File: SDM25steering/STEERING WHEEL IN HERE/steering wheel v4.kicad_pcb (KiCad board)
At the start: 4 copper layers, 162.2 x 126.4 mm, 125 parts, among them J1 JST_EH_S2B-EH_1x02_P2.50mm_Ho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, J2 JST_EH_S2B-EH_1x02_P2.50mm_Ho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, J3 Conn_01x04_Socket, J4 Conn_ARM_SWD_TagConnect_TC2030, J5 USB_B_Micro, U1 STM32F405RGT6, U2 MIC37100-3.3WS, U3 SN65HVD230, U4 TLC59108F, U5 ADR425BRZ, U6 24LC01BT-E/LT, U6 TPS2116, U7 ADC128S102, U8 USBLC6-2SC6, Y1 12MHz

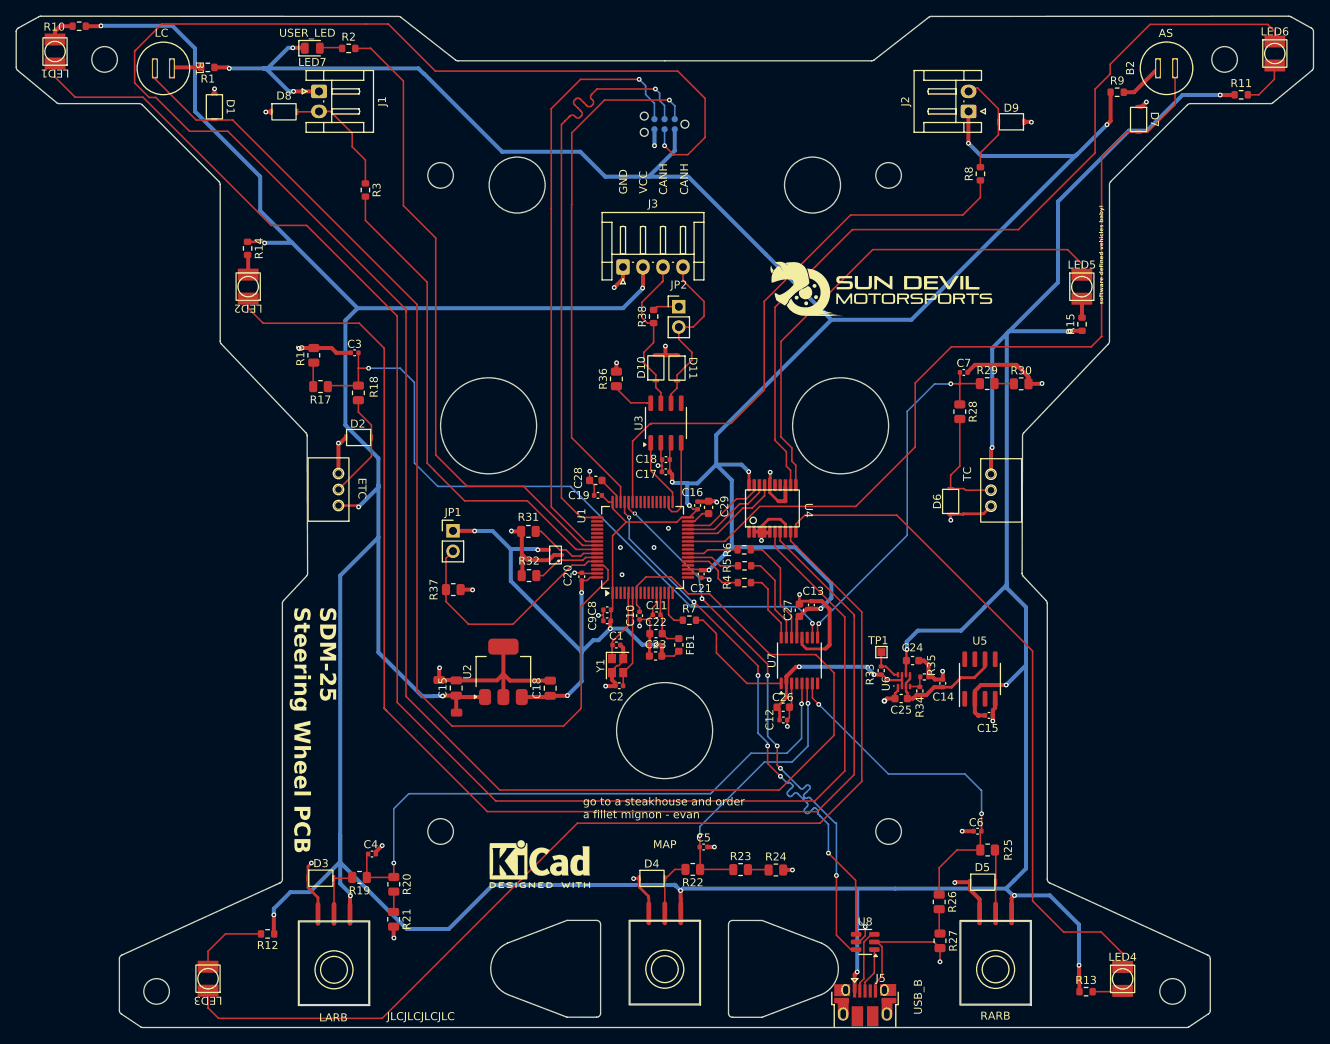
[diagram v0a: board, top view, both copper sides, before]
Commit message: SDM-24 Logger TVS diodes
TVS protection added on all analog inputs. Also built out for manufacture files.
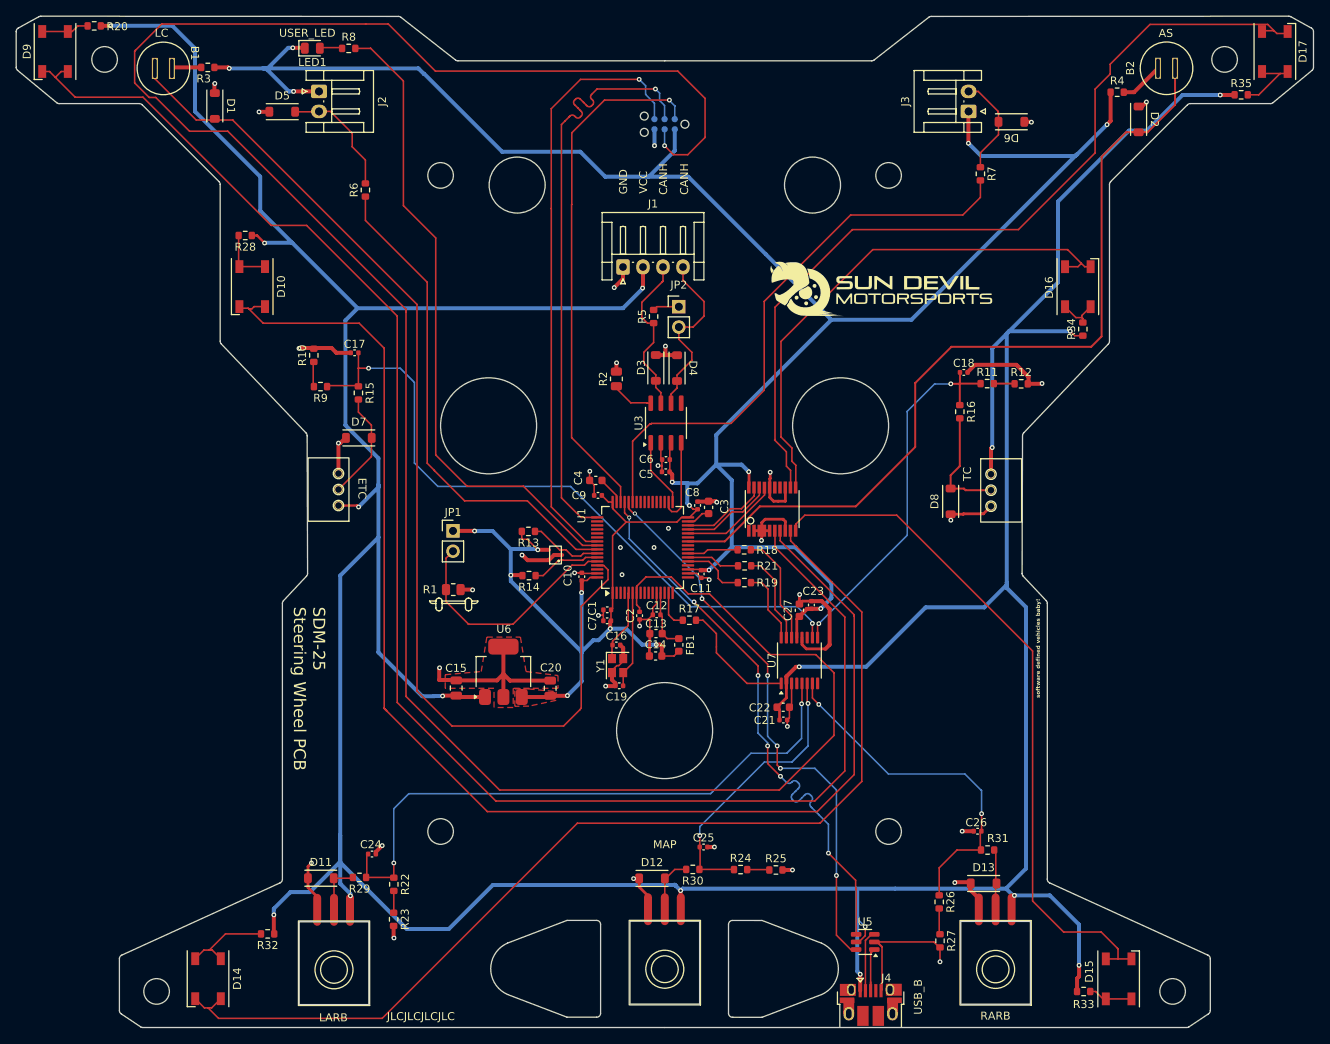
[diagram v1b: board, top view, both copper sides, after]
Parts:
- removed ? (x2): , 
- removed the C14 at (186.7, 109.0)
- removed the C15 at (192.5, 113.0)
- removed the C24 at (182.9, 106.1)
- removed the C25 at (181.5, 110.9)
- removed the R33 at (179.0, 107.4)
- removed the R34 at (183.8, 109.9)
- removed the R35 at (184.4, 108.2)
- removed REF**: KiCad-Logo2_5mm_SilkScreen, Symbol:KiCad-Logo2_5mm_SilkScreen
- removed TP1: ST_5VA, TestPoint:TestPoint_Pad_1.0x1.0mm
- removed the U4 at (165.4, 87.1)
- removed the U5 at (191.3, 108.4)
- removed the U6 at (180.4, 108.7)
- added TLC59108F1: U4, Library:TLC59108F, F.Cu at (165.4, 87.2)
- C17: renamed from C3; value 100nF -> 100n
- C18: renamed from C7; value 100nF -> 100n
- C24: renamed from C4; value 100nF -> 100n
- C25: renamed from C5; value 100nF -> 100n
- C26: renamed from C6; value 100nF -> 100n
- D1: footprint TVS Diode:SOD-123FL -> Library:SOD-123FL
- D10: renamed from LED2; value green -> LTST-C235KGKRKT; footprint LED:LR T66F-AABB-1-1 -> LED_SMD:LED_Cree-PLCC4_5x5mm_CW
- D11: renamed from D3; footprint TVS Diode:SOD-123FL -> Library:SOD-123FL
- D12: renamed from D4; footprint TVS Diode:SOD-123FL -> Library:SOD-123FL
- D13: renamed from D5; footprint TVS Diode:SOD-123FL -> Library:SOD-123FL
- D14: renamed from LED3; value green -> LTST-C235KGKRKT; footprint LED:LR T66F-AABB-1-1 -> LED_SMD:LED_Cree-PLCC4_5x5mm_CW
- D15: renamed from LED4; value green -> LTST-C235KGKRKT; footprint LED:LR T66F-AABB-1-1 -> LED_SMD:LED_Cree-PLCC4_5x5mm_CW
- D16: renamed from LED5; value green -> LTST-C235KGKRKT; footprint LED:LR T66F-AABB-1-1 -> LED_SMD:LED_Cree-PLCC4_5x5mm_CW
- D17: renamed from LED6; value blue -> LTST-C235KGKRKT; footprint LED:LR T66F-AABB-1-1 -> LED_SMD:LED_Cree-PLCC4_5x5mm_CW
- D2: renamed from D7; footprint TVS Diode:SOD-123FL -> Library:SOD-123FL
- D3: renamed from D10; footprint TVS Diode:SOD-123FL -> Library:SOD-123FL
- D4: renamed from D11; footprint TVS Diode:SOD-123FL -> Library:SOD-123FL
- D5: renamed from D8; footprint TVS Diode:SOD-123FL -> Library:SOD-123FL
- D6: renamed from D9; footprint TVS Diode:SOD-123FL -> Library:SOD-123FL
- D7: renamed from D2; footprint TVS Diode:SOD-123FL -> Library:SOD-123FL
- D8: renamed from D6; footprint TVS Diode:SOD-123FL -> Library:SOD-123FL
- D9: renamed from LED1; value red -> LTST-C235KGKRKT; footprint LED:LR T66F-AABB-1-1 -> LED_SMD:LED_Cree-PLCC4_5x5mm_CW
- J2: renamed from J1; value JST_EH_S2B-EH_1x02_P2.50mm_Horizontal -> Conn_01x02
- J3: renamed from J2; value JST_EH_S2B-EH_1x02_P2.50mm_Horizontal -> Conn_01x02
- POT4, POT5: footprint Dial Potentiometer:P081N-271F2CBR10K -> Library:P081N-271F2CBR10K
- R10: renamed from R16; value 1000 -> 1k; footprint Resistor_SMD:R_0805_2012Metric -> Resistor_SMD:R_0603_1608Metric
- R11: renamed from R29; value 1000 -> 1k; footprint Resistor_SMD:R_0805_2012Metric -> Resistor_SMD:R_0603_1608Metric
- R12: renamed from R30; value 1000 -> 1k; footprint Resistor_SMD:R_0805_2012Metric -> Resistor_SMD:R_0603_1608Metric
- R13: renamed from R31; footprint Resistor_SMD:R_0805_2012Metric -> Resistor_SMD:R_0603_1608Metric
- R14: renamed from R32; footprint Resistor_SMD:R_0805_2012Metric -> Resistor_SMD:R_0603_1608Metric
- R15: renamed from R18; value 1000 -> 1k; footprint Resistor_SMD:R_0805_2012Metric -> Resistor_SMD:R_0603_1608Metric
- R16: renamed from R28; value 1000 -> 1k; footprint Resistor_SMD:R_0805_2012Metric -> Resistor_SMD:R_0603_1608Metric
- R22: renamed from R20; value 1000 -> 1k; footprint Resistor_SMD:R_0805_2012Metric -> Resistor_SMD:R_0603_1608Metric
- R23: renamed from R21; value 1000 -> 1k; footprint Resistor_SMD:R_0805_2012Metric -> Resistor_SMD:R_0603_1608Metric
- R24: renamed from R23; value 1000 -> 1k; footprint Resistor_SMD:R_0805_2012Metric -> Resistor_SMD:R_0603_1608Metric
- R25: renamed from R24; value 1000 -> 1k; footprint Resistor_SMD:R_0805_2012Metric -> Resistor_SMD:R_0603_1608Metric
- R26, R27: value 1000 -> 1k; footprint Resistor_SMD:R_0805_2012Metric -> Resistor_SMD:R_0603_1608Metric
- R29: renamed from R19; value 1000 -> 1k; footprint Resistor_SMD:R_0805_2012Metric -> Resistor_SMD:R_0603_1608Metric
- R30: renamed from R22; value 1000 -> 1k; footprint Resistor_SMD:R_0805_2012Metric -> Resistor_SMD:R_0603_1608Metric
- R31: renamed from R25; value 1000 -> 1k; footprint Resistor_SMD:R_0805_2012Metric -> Resistor_SMD:R_0603_1608Metric
- R9: renamed from R17; value 1000 -> 1k; footprint Resistor_SMD:R_0805_2012Metric -> Resistor_SMD:R_0603_1608Metric
- moved R20 1.88 mm to (80.6, 26.8)
- moved R28 1.64 mm to (99.5, 53.0), turned to 180 degrees
- moved J4 0.70 mm to (177.7, 149.2)
- moved R34 0.62 mm to (204.2, 64.7)
- moved D10 0.50 mm to (100.4, 59.4), turned to 90 degrees
- moved D15 0.50 mm to (208.7, 145.9), turned to -90 degrees
- moved D16 0.50 mm to (203.6, 59.4), turned to -90 degrees
- moved R33 0.31 mm to (204.3, 147.5)
- moved D17 0.25 mm to (228.2, 30.0), turned to -90 degrees
- moved D5 0.22 mm to (104.1, 37.5)
- moved D13 0.19 mm to (191.8, 134.0)
- moved D1 0.12 mm to (95.7, 36.8)
- moved D7 0.06 mm to (113.7, 78.3)
- turned D14 to 90 degrees
- turned D9 to 90 degrees
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- renumbered C8 to C1, C20 to C10, C21 to C11, C11 to C12, C22 to C13, C23 to C14, C1 to C16, C2 to C19, C10 to C2, C18 to C20, C12 to C21, C26 to C22, C13 to C23, C29 to C3, C28 to C4, C17 to C5, C18 to C6, C9 to C7, C16 to C8, C19 to C9, H5 to H2, H2 to H3, H6 to H4, H3 to H5, H7 to H6, H4 to H7, J3 to J1, J5 to J4, J4 to J5, LED7 to LED1, R37 to R1, R7 to R17, R6 to R18, R4 to R19, R36 to R2, R10 to R20, R5 to R21, R14 to R28, R1 to R3, R12 to R32, R13 to R33, R15 to R34, R11 to R35, R9 to R4, R38 to R5, R3 to R6, R8 to R7, R2 to R8, U6 to U4, U8 to U5, U2 to U6
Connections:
- net I2C1_SCL renamed /I2C1_SCL
- net I2C1_SDA renamed /I2C1_SDA
- net net1 renamed Net-(R22-Pad2)
- net net2 renamed Net-(R24-Pad2)
- net net3 renamed Net-(R26-Pad2)
- net net5 renamed Net-(R11-Pad2)
- net net6 renamed Net-(R10-Pad1)
- C21 pad 1: +5VA -> VCC
- C22 pad 1: +5VA -> VCC
- D10 pad 2: Net-(D12-A) -> Net-(D10-A1)
- D14 pad 2: Net-(D13-A) -> Net-(D14-A1)
- D15 pad 2: Net-(D14-A) -> Net-(D15-A1)
- D16 pad 2: Net-(D16-A) -> Net-(D16-A1)
- D17 pad 2: Net-(D15-A) -> Net-(D17-A1)
- D5 pad 2: B3 -> /B3
- D6 pad 2: B4 -> /B4
- D9 pad 2: Net-(D11-A) -> Net-(D9-A1)
- J2 pad 2: B3 -> /B3
- J3 pad 2: B4 -> /B4
- R13 pad 2: GND -> +3.3V
- R14 pad 2: GND -> +3.3V
- R20 pad 2: Net-(D11-A) -> Net-(D9-A1)
- R28 pad 2: Net-(D12-A) -> Net-(D10-A1)
- R32 pad 2: Net-(D13-A) -> Net-(D14-A1)
- R33 pad 2: Net-(D14-A) -> Net-(D15-A1)
- R34 pad 2: Net-(D16-A) -> Net-(D16-A1)
- R35 pad 2: Net-(D15-A) -> Net-(D17-A1)
- R6 pad 1: B3 -> /BUTTON3
- R6 pad 2: BUTTON3 -> /B3
- R7 pad 1: B4 -> /BUTTON4
- R7 pad 2: BUTTON4 -> /B4
- U1 pad 16: (no net) -> unconnected-(U3-PA2-Pad16)
- U1 pad 17: (no net) -> unconnected-(U3-PA3-Pad17)
- U1 pad 20: (no net) -> unconnected-(U3-PA4-Pad20)
- U1 pad 24: /G0_1 -> unconnected-(U3-PC4-Pad24)
- U1 pad 25: (no net) -> unconnected-(U3-PC5-Pad25)
- U1 pad 3: (no net) -> unconnected-(U3-PC14-Pad3)
- U1 pad 35: (no net) -> unconnected-(U3-PB14-Pad35)
- U1 pad 36: /FAN -> unconnected-(U3-PB15-Pad36)
- U1 pad 40: (no net) -> unconnected-(U3-PC9-Pad40)
- U1 pad 41: (no net) -> unconnected-(U3-PA8-Pad41)
- U1 pad 42: (no net) -> unconnected-(U3-PA9-Pad42)
- U1 pad 43: BUTTON4 -> /BUTTON4
- U1 pad 50: (no net) -> unconnected-(U3-PA15-Pad50)
- U1 pad 51: (no net) -> unconnected-(U3-PC10-Pad51)
- U1 pad 57: BUTTON3 -> /BUTTON3
- U7 pad 2: +5VA -> VCC
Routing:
- net BUTTON4: track 72.3 -> 0.00 mm
- net /BUTTON4: track 0.00 -> 72.3 mm
- net BUTTON3: track 62.3 -> 0.00 mm
- net /BUTTON3: track 0.00 -> 62.3 mm
- net +5VA: track 23.1 -> 0.00 mm, vias 2 -> 0
- net netA: track 15.6 -> 0.00 mm
- net B3: track 15.0 -> 0.00 mm
- net /B3: track 0.00 -> 15.0 mm
- net GND: track 202.6 -> 188.3 mm, vias 43 -> 40
- net B4: track 13.0 -> 0.00 mm
- net /B4: track 0.00 -> 12.7 mm
- net Net-(D14-A1): track 0.00 -> 11.4 mm
- net Net-(D13-A): track 9.35 -> 0.00 mm
- net Net-(D17-A1): track 0.00 -> 8.34 mm
- net Net-(D10-A1): track 0.00 -> 7.55 mm
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- added copper zone on F.Cu, net +3.3V
- added copper zone on F.Cu, net GND
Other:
- board text removed: "D10"
- board text removed: "D3"
- board text removed: "D4"
- board text removed: "D5"

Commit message: IMU + Telemetry + Steering Wheel
Final manufacturing outputs
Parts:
- D1, D11, D12, D13, D2, D5, D6, D7, D8: footprint Library:SOD-123FL -> Diode_SMD:D_SOD-323
- moved D1 0.69 mm to (95.7, 37.5)
- moved D13 0.51 mm to (192.2, 133.8)
- moved D2 0.51 mm to (211.2, 39.0)
- moved D7 0.50 mm to (114.2, 78.3)
- moved D6 0.47 mm to (194.8, 38.8)
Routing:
- net GND: track 188.3 -> 193.7 mm
- net /D+: track 6.55 -> 5.34 mm
- net /POT_TC: track 14.3 -> 15.2 mm
- net /B3: track 15.0 -> 15.8 mm
- net /POT_MAP: track 7.40 -> 8.08 mm
- net /POT_LARB: track 6.84 -> 7.39 mm

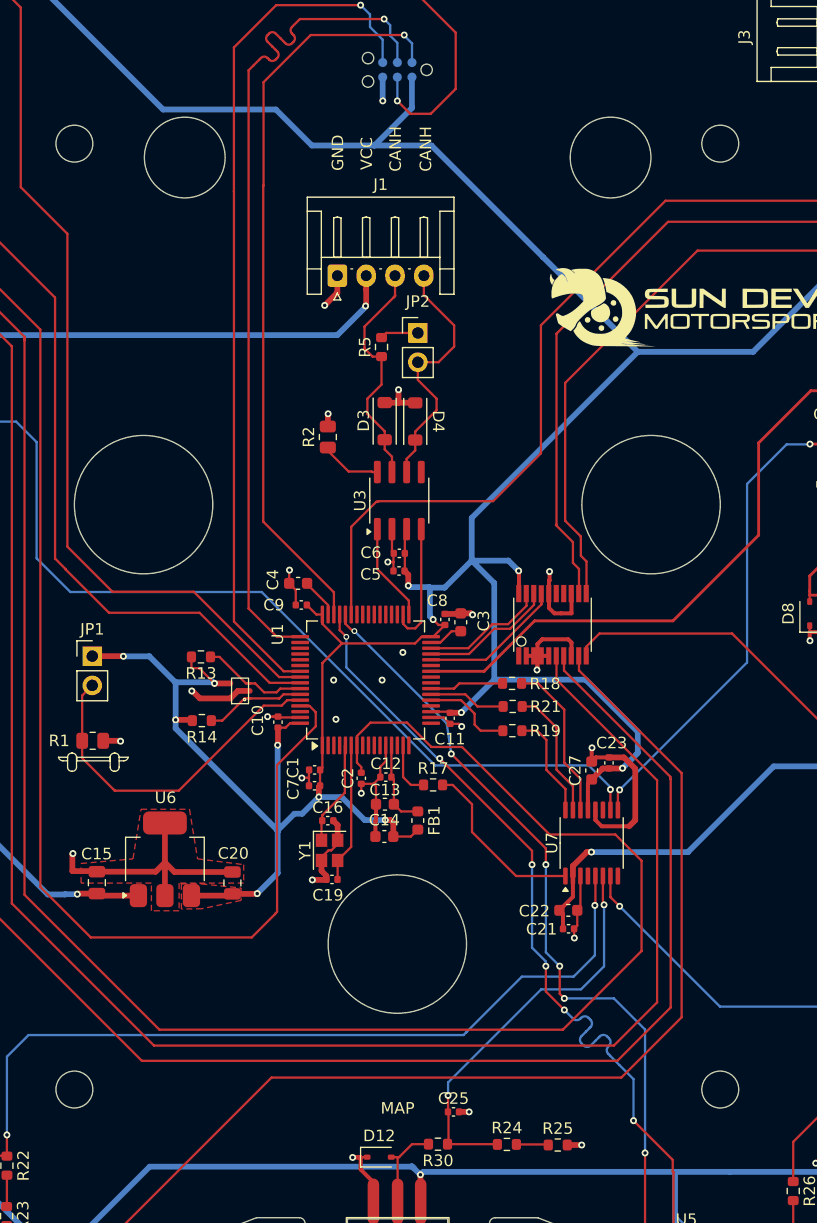
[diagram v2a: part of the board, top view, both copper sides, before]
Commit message: drs/mcpm fix
changing folder name

also uploading WIP steering wheel revision
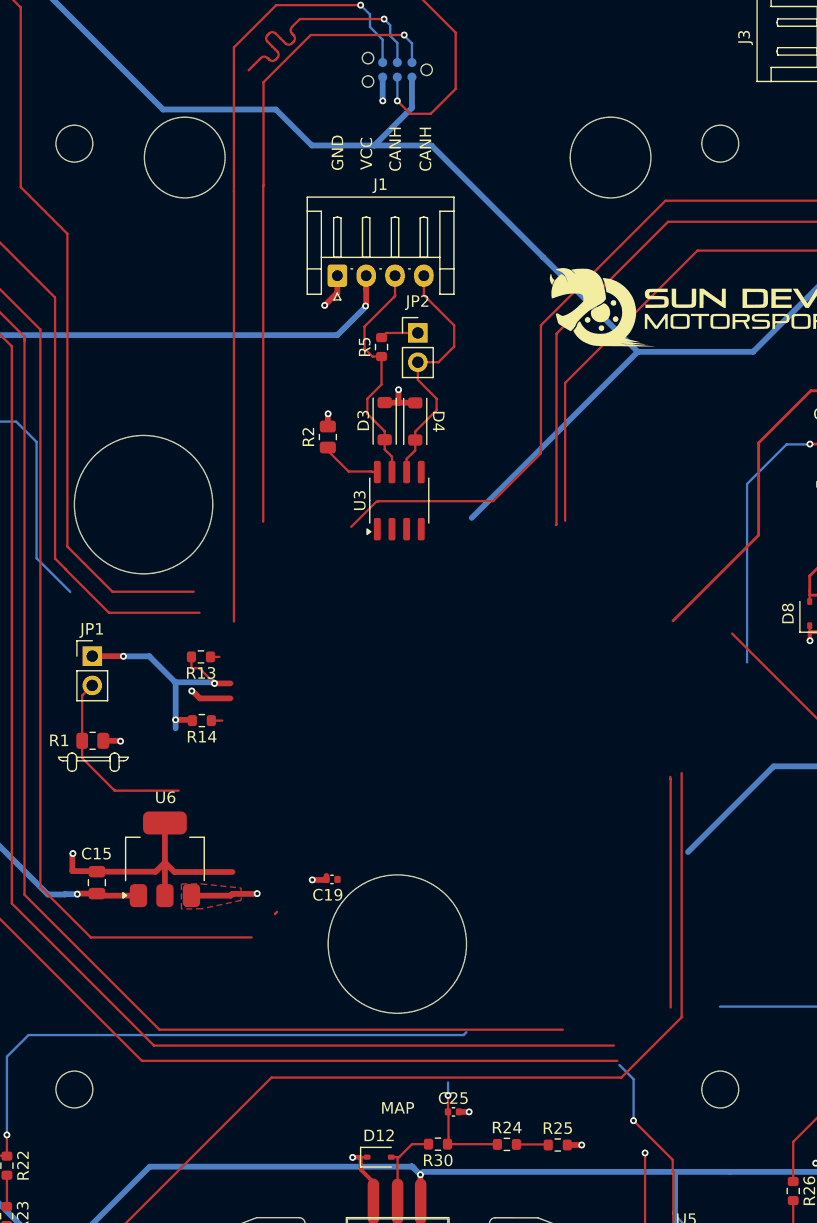
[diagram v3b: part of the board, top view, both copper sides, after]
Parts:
- removed C1, C10, C11, C12, C2, C21, C23, C5, C6, C7, C8, C9: 100nF, Capacitor_SMD:C_0402_1005Metric
- removed C13, C14, C22, C27: 1uF, Capacitor_SMD:C_0603_1608Metric
- removed C16: 10pF, Capacitor_SMD:C_0402_1005Metric
- removed C20: 10uF, Capacitor_SMD:C_0805_2012Metric
- removed C3, C4: 2.2uF, Capacitor_SMD:C_0603_1608Metric
- removed FB1: 120R, Inductor_SMD:L_0603_1608Metric
- removed R17, R18, R19, R21: 220, Resistor_SMD:R_0603_1608Metric
- removed TLC59108F1: U4, Library:TLC59108F
- removed U1: STM32F405RGT6, Package_QFP:LQFP-64_10x10mm_P0.5mm
- removed U4: 24LC01BT-E/LT, Voltage Regulator:SC-70-5
- removed U7: ADC128S102, Package_SO:TSSOP-16_4.4x5mm_P0.65mm
- removed Y1: 12MHz, Crystal:Crystal_SMD_2520-4Pin_2.5x2.0mm
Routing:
- net +3.3V: track 368.0 -> 227.2 mm, vias 17 -> 9
- net GND: track 193.7 -> 121.9 mm, vias 40 -> 25
- net /USB_D-: track 70.6 -> 10.7 mm, vias 6 -> 1
- net /AIN6: track 85.7 -> 29.9 mm, vias 2 -> 1
- net /USB_D+: track 70.4 -> 16.9 mm, vias 6 -> 1
- net /SWCLK: track 74.5 -> 22.3 mm
- net /NRST: track 290.7 -> 239.8 mm
- net /LED1: track 203.6 -> 164.5 mm
- net /AIN2: track 35.1 -> 9.53 mm, vias 2 -> 1
- net /BUTTON_LC: track 137.6 -> 114.5 mm
- net /BUTTON_AS: track 106.1 -> 83.3 mm
- net /LED2: track 168.5 -> 147.6 mm
- net /AIN1: track 76.4 -> 55.6 mm, vias 2 -> 1
- net /AIN5: track 47.5 -> 30.1 mm, vias 2 -> 1
- net VCC: track 548.8 -> 532.2 mm, vias 16 -> 15
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- removed copper zone on F.Cu, net GND
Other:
- outline, holes or cut-outs redrawn
